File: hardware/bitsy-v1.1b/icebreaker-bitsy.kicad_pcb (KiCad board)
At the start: 4 copper layers, 36 x 18 mm, 99 parts, among them J1 USB_C, P0 0, P1 1, P10 10, P11 11, P12 12, P13 13, P14 14, P15 15, P16 16, P17 17, P18 18, P19 19, P2 2, P20 20, P21 21, P22 22, P23 23, P24 GND, P25 GND, P26 GND, P27 3V3, P28 3V3, P29 VIN, P3 3, P30 CDONE, P31 CRESET, P32 UP, P33 UP, P34 UP, P35 UP, P36 CS, P37 SCK, P38 MISO, P39 MOSI, P4 4, P40 IO3, P41 IO2, P5 5, P6 6, P7 7, P8 8, P9 9, SW1 TACT, U1 USBLC6-2, U2 TLV75533PDRV, U3 TLV75512PDRV, U4 LY68L6400, U5 W25Q128JVxxM, U6 ICE40UP5K-SG48, X1 12MHz

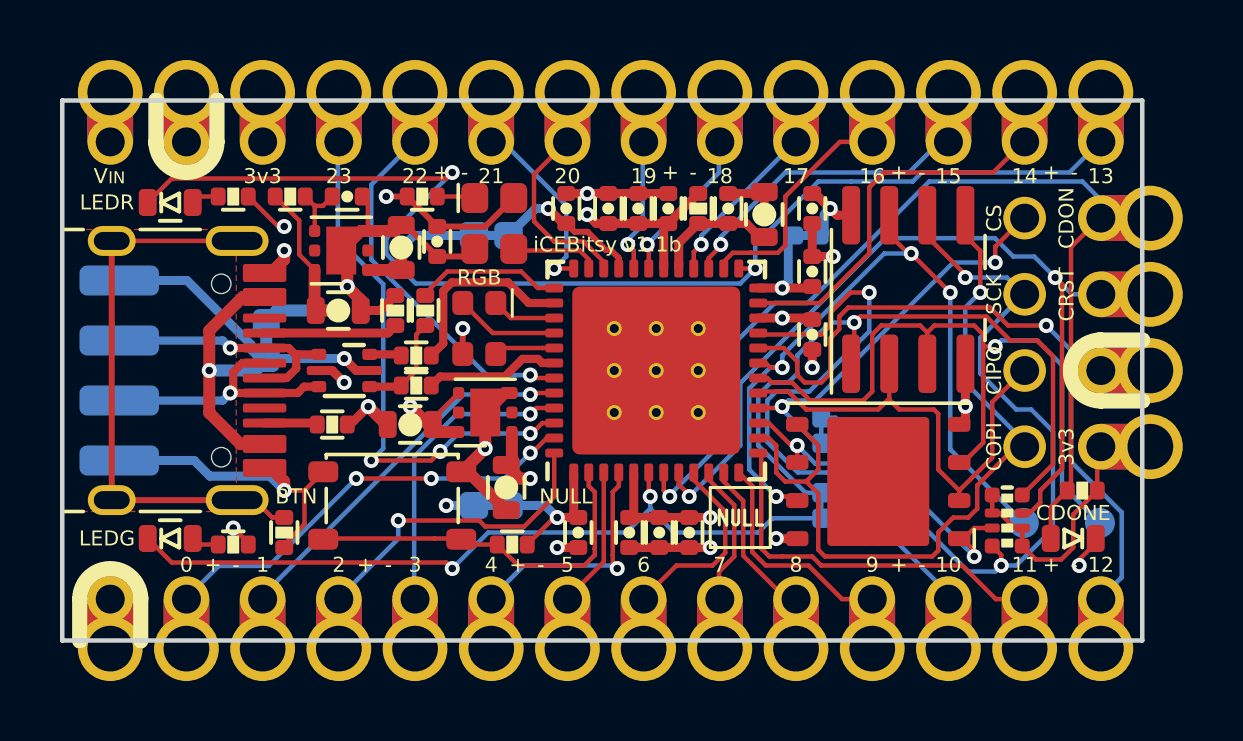
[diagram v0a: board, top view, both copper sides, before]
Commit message: Rerouted USB Diff Pair and added BCop GND Pour
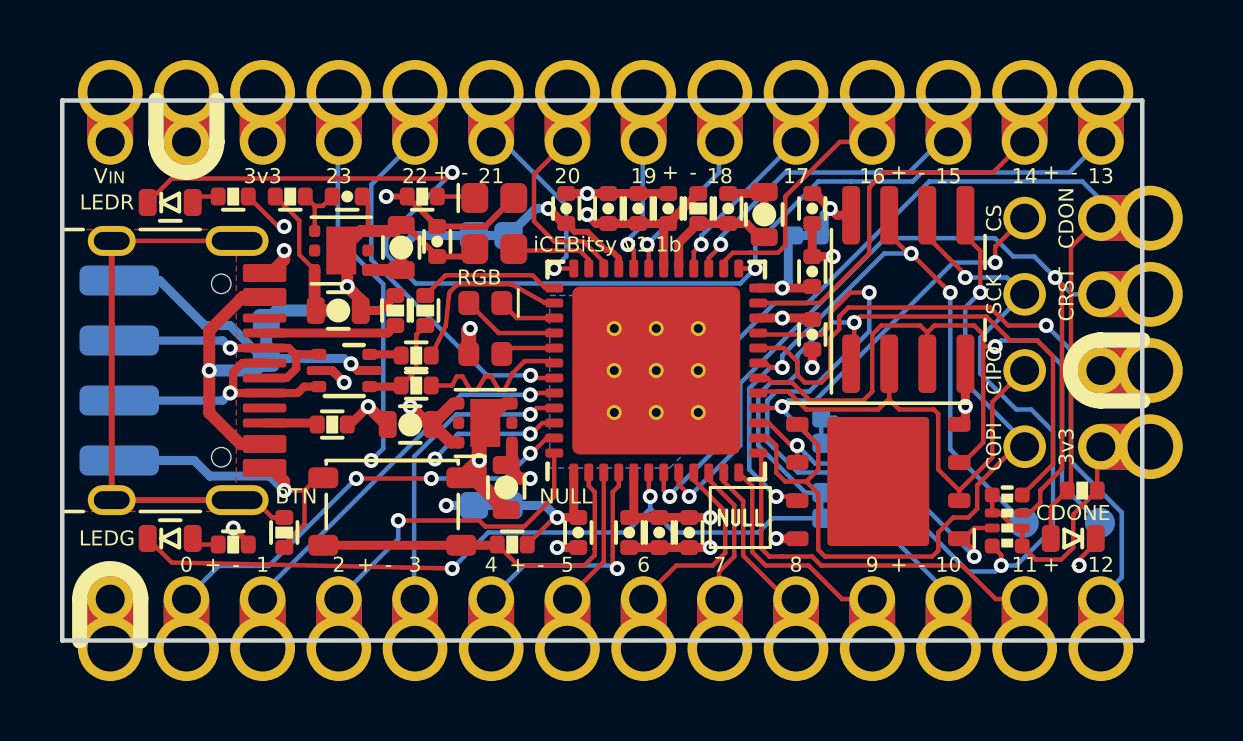
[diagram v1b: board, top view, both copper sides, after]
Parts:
- LOGO1: footprint pkl_logos:null_Logo_SilkS_6.5mm -> pkl_logos:1b2_Logo_SilkS_6.5mm
- U3: value TLV75512PDRV -> TLV73312PDRV
- moved U3 0.35 mm to (46.1, 51.8)
- moved D4 0.20 mm to (46.1, 48.6)
- moved SW1 0.20 mm to (43.0, 54.7)
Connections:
- net /USB_N renamed /USB-
- net /USB_P renamed /USB+
- U2 pad 2: Net-(U2-Pad2) -> (no net)
- U2 pad 5: Net-(U2-Pad5) -> (no net)
- U3 pad 2: Net-(U3-Pad2) -> (no net)
- U3 pad 5: Net-(U3-Pad5) -> (no net)
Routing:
- net /USB+: track 4.52 -> 5.62 mm
- added copper zone on B.Cu, net GND
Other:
- net class Default removed
- net class S50 removed
- net class USB-D90 removed

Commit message: Exploring DiffPair Routing
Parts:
- removed R9: 10k, pkl_dipol:R_Array_Convex_4x0402
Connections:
- net /IOB_8a renamed /IOB_DP2+
- net /IOB_9b renamed /IOB_DP2-
